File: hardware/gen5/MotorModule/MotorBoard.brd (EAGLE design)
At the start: 160 x 100 mm, 51 parts, among them IC2 3.3V REG, M1O1 TEST_PT, M1O2 TEST_PT, M1O3 TEST_PT

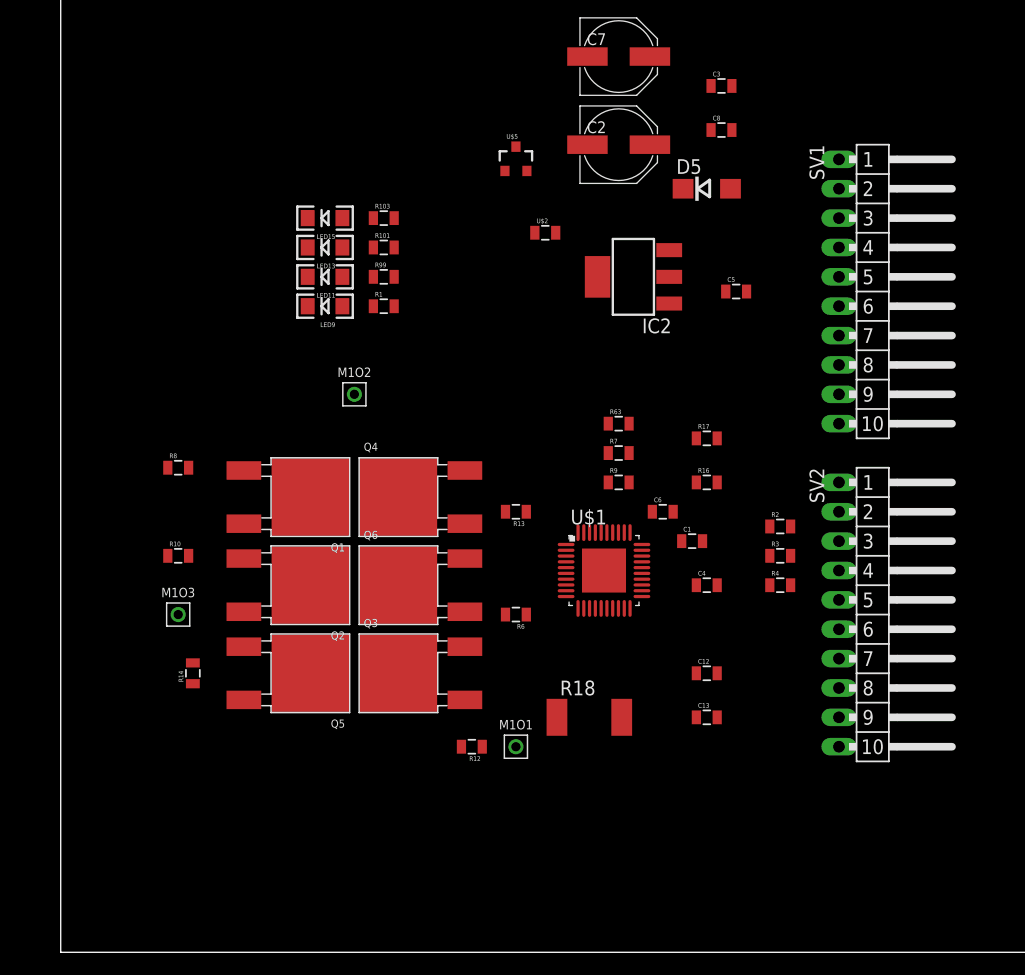
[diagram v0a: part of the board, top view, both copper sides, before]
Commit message: Working on motor board layout - should be done soon
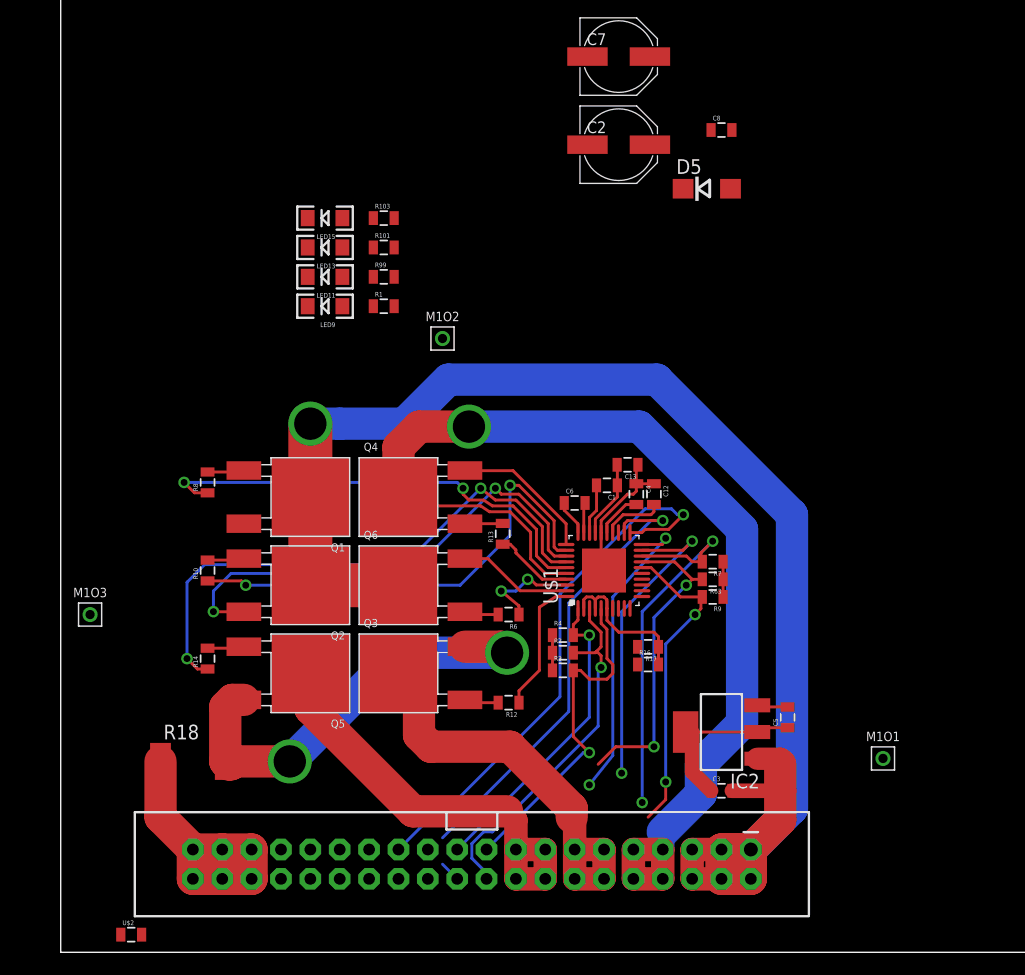
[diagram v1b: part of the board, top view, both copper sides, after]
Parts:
- removed SV1, SV2: (no value), con-lstb:MA10-1W
- removed U$5: MCP9700SMD, SparkFun-Sensors:SOT23-3
- added J1: M20X2SHROUDED, SparkFun-Connectors:2X20_SHROUDED
- moved U$2 70.5 mm to (6.10, 1.52)
- moved C3 61.0 mm to (57.1, 14.0)
- moved IC2 40.1 mm to (57.1, 19.1)
- moved C5 37.1 mm to (62.9, 20.3), turned to 90 degrees
- moved R18 34.5 mm to (11.4, 16.5)
- moved M1O1 31.8 mm to (71.1, 16.8)
- moved C13 22.9 mm to (49.0, 42.2), turned to 180 degrees
- moved R2 21.7 mm to (43.4, 25.9)
- moved R3 21.2 mm to (43.4, 24.4)
- moved R4 19.3 mm to (43.4, 27.4)
- moved R17 18.7 mm to (50.8, 26.4), turned to 180 degrees
- moved R16 16.5 mm to (50.8, 24.9)
- moved C12 16.2 mm to (51.3, 39.6), turned to 270 degrees
- moved R63 15.7 mm to (56.4, 32.3), turned to 180 degrees
- moved R9 12.8 mm to (56.4, 30.7), turned to 180 degrees
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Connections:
- removed net TSENSE: U$5.2
- net 12V: now also J1.1, J1.2, J1.3, J1.4, J1.5, J1.6; no longer SV1.10, SV1.6, SV1.7, SV1.8, SV1.9
- net 12VGND: now also J1.35, J1.36, J1.37, J1.38, J1.39, J1.40; no longer SV1.1, SV1.2, SV1.3, SV1.4, SV1.5
- net 3.3V: no longer U$5.1
- net 5V: now also J1.23
- net BRAKE: now also J1.27; no longer SV2.6
- net DIR: now also J1.25; no longer SV2.7
- net ENABLE: now also J1.22; no longer SV2.4
- net FAULTN: now also J1.31; no longer SV2.2
- net GND: no longer U$5.3
- net HALLOUT: now also J1.24; no longer SV2.3
- net LOCKN: now also J1.26; no longer SV2.1
- net M1H1: now also J1.19, R3.2; no longer R2.2, SV2.9
- net M1H2: now also J1.20, R2.2; no longer R3.2, SV2.10
- net M1H3: now also J1.21; no longer SV2.8
- net M1O1: now also J1.11, J1.12, J1.13, J1.14
- net M1O2: now also J1.10, J1.7, J1.8, J1.9
- net M1O3: now also J1.15, J1.16, J1.17, J1.18
- net PWM: now also J1.29; no longer SV2.5
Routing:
- net 12V: track 0.00 -> 142.2 mm, vias 0 -> 2
- net M1O2: track 0.00 -> 97.7 mm, vias 0 -> 1
- net M1O3: track 0.00 -> 79.9 mm, vias 0 -> 2
- net O1: track 0.00 -> 51.4 mm, vias 0 -> 2
- net N$17: track 0.00 -> 48.8 mm, vias 0 -> 2
- net DIR: track 0.00 -> 47.5 mm, vias 0 -> 1
- net M1O1: track 0.00 -> 45.6 mm
- net ENABLE: track 0.00 -> 41.9 mm, vias 0 -> 1
- net N$21: track 0.00 -> 40.9 mm, vias 0 -> 2
- net N$20: track 0.00 -> 40.3 mm, vias 0 -> 2
- net LOCKN: track 0.00 -> 32.8 mm, vias 0 -> 2
- net M1H2: track 0.00 -> 31.8 mm, vias 0 -> 1
- net M1H1: track 0.00 -> 30.0 mm, vias 0 -> 1
- net PWM: track 0.00 -> 27.3 mm, vias 0 -> 2
- net HALLOUT: track 0.00 -> 27.2 mm, vias 0 -> 2
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
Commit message: Motor board finished - needs review
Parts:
- removed M1O1, M1O2, M1O3: TEST_PT, gen3:TESTING_PT
- moved U$2 55.4 mm to (57.8, 21.5), turned to 270 degrees
- moved LED11 43.7 mm to (50.3, 24.4)
- moved R99 43.2 mm to (54.6, 24.4)
- moved LED13 40.4 mm to (54.1, 35.3)
- moved LED15 40.3 mm to (54.1, 38.1), turned to 0 degrees
- moved R101 40.1 mm to (54.6, 31.0), turned to 270 degrees
- moved D5 38.9 mm to (58.4, 27.2), turned to 270 degrees
- moved R103 34.6 mm to (50.3, 37.1), turned to 270 degrees
- moved C7 34.3 mm to (37.3, 45.0)
- moved LED9 27.5 mm to (47.0, 42.7)
- moved C8 27.5 mm to (43.9, 47.0), turned to 180 degrees
- moved C2 26.4 mm to (55.4, 44.5), turned to 180 degrees
- moved R1 26.2 mm to (48.5, 39.6), turned to 270 degrees
- moved R14 8.77 mm to (4.06, 23.9), flipped to the bottom
- moved R6 5.79 mm to (33.5, 26.7)
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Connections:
- net 12VGND: now also J1.22, J1.33, J1.34
- net ENABLE: now also J1.30; no longer J1.22
- net M1O1: no longer M1O1.P$1
- net M1O2: no longer M1O2.P$1
- net M1O3: no longer M1O3.P$1
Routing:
- net 12VGND: track 26.6 -> 183.1 mm
- net 5V: track 8.36 -> 79.7 mm, vias 0 -> 3
- net GND: track 27.1 -> 83.1 mm, vias 0 -> 2
- net FAULTN: track 27.1 -> 73.0 mm, vias 2 -> 3
- net M1O2: track 97.7 -> 136.5 mm
- net PWM: track 27.3 -> 63.8 mm, vias 2 -> 1
- net HALLOUT: track 27.2 -> 63.1 mm, vias 2 -> 4
- net BRAKE: track 26.2 -> 60.6 mm, vias 2 -> 1
- net O1: track 51.4 -> 84.3 mm, vias 2 -> 3
- net LOCKN: track 32.8 -> 65.2 mm
- net 12V: track 142.2 -> 171.6 mm, vias 2 -> 4
- net ENABLE: track 41.9 -> 70.0 mm, vias 1 -> 3
- net M1O3: track 79.9 -> 101.6 mm
- net M1O1: track 45.6 -> 61.9 mm, vias 0 -> 2
- net 3.3V: track 5.72 -> 20.1 mm
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- added copper zone on layer 1, net 12VGND
- added copper zone on layer 16, net 12VGND
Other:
- board size 160 x 100 mm -> 60.9 x 49.7 mm

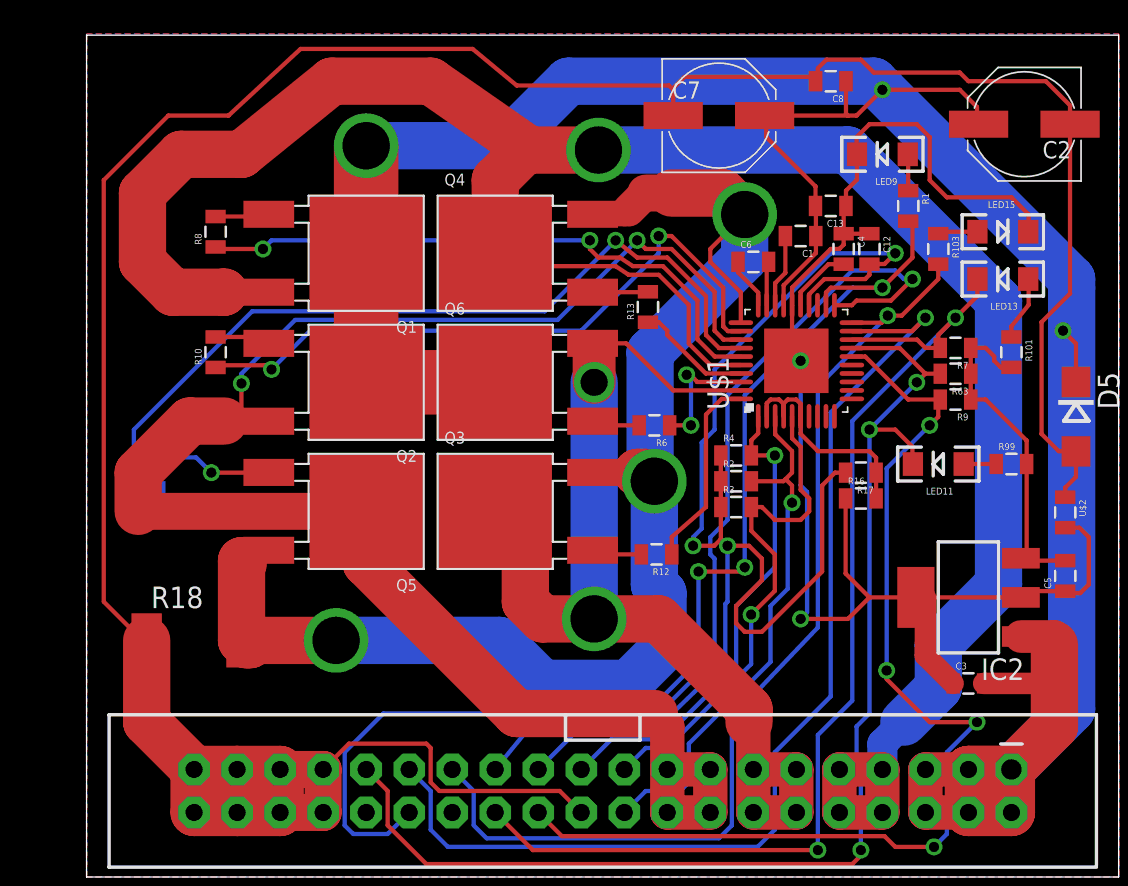
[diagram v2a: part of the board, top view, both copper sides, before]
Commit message: few minor motor board fixes
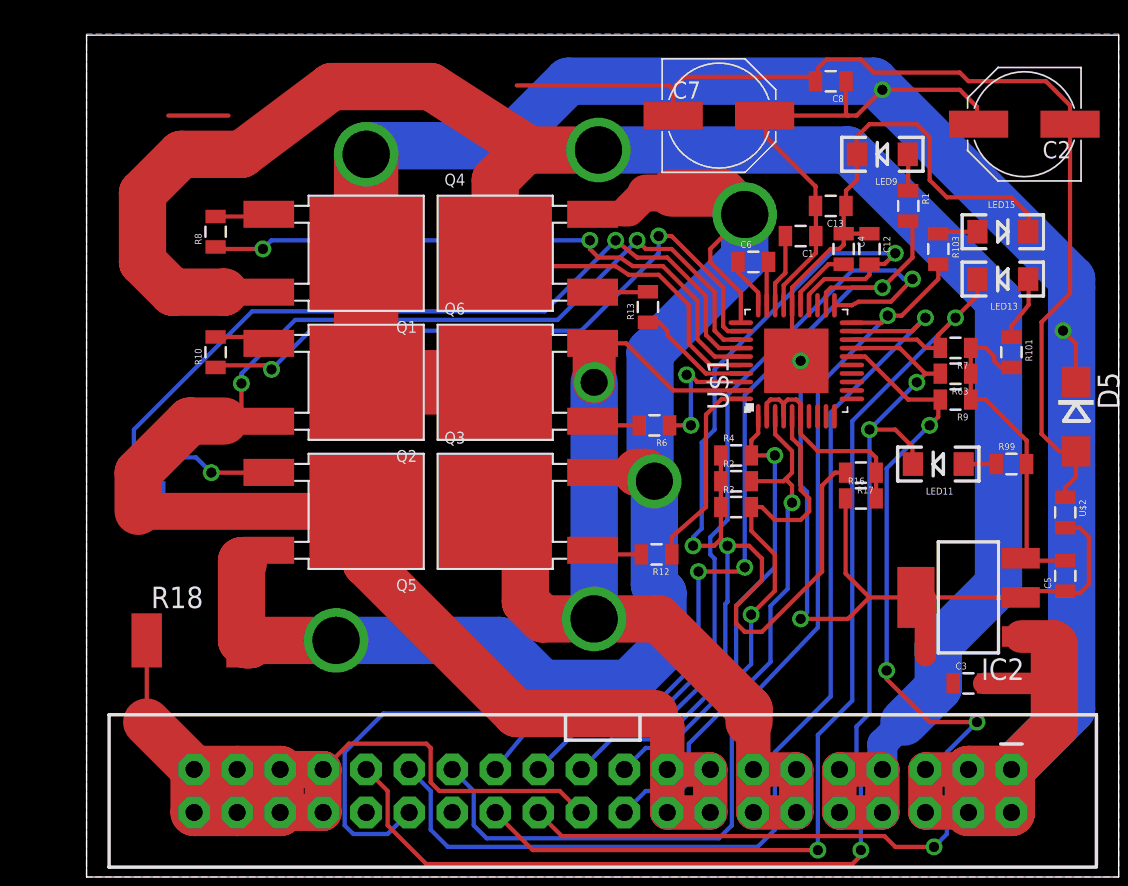
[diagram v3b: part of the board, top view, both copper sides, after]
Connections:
- net 12VGND: now also C3.1
- net GND: no longer C3.1
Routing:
- net 12VGND: track 183.1 -> 125.0 mm
- net GND: track 83.1 -> 80.8 mm
- net 12V: track 171.6 -> 171.3 mm, vias 4 -> 3
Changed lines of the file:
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@@
 <contactref element="C5" pad="1"/>
 <contactref element="U$2" pad="2"/>
-<contactref element="C3" pad="1"/>
 <contactref element="LED9" pad="C"/>
 <contactref element="LED15" pad="C"/>
 <wire x1="48.971" y1="16.51" x2="49.53" y2="16.51" width="0.254" layer="1"/>
 <wire x1="49.53" y1="16.51" x2="55.1688" y2="16.51" width="0.254" layer="1"/>
-<wire x1="51.17" y1="11.43" x2="49.53" y2="13.07" width="1.27" layer="1"/>
 <wire x1="49.53" y1="13.07" x2="49.53" y2="16.002" width="1.27" layer="1"/>
 <wire x1="49.53" y1="16.002" x2="49.53" y2="16.51" width="1.27" layer="1"/>
@@
 <wire x1="24.13" y1="29.21" x2="16.51" y2="29.21" width="3.81" layer="1"/>
 <wire x1="16.51" y1="29.21" x2="16.51" y2="36.83" width="3.81" layer="1"/>
-<wire x1="16.51" y1="36.83" x2="16.51" y2="43.18" width="3.81" layer="1"/>
-<via x="16.51" y="43.18" extent="1-16" drill="2.8"/>
+<wire x1="16.51" y1="36.83" x2="16.51" y2="42.672" width="3.81" layer="1"/>
+<via x="16.51" y="42.672" extent="1-16" drill="2.8"/>
 <wire x1="41.16" y1="33.759" x2="41.16" y2="34.937" width="0.254" layer="1"/>
 <wire x1="41.16" y1="34.937" x2="43.064" y2="36.841" width="0.254" layer="1"/>
@@
 <wire x1="54.356" y1="6.35" x2="54.61" y2="6.096" width="2.794" layer="1"/>
 <wire x1="54.61" y1="6.096" x2="54.61" y2="6.35" width="2.794" layer="1"/>
-<via x="54.61" y="6.35" extent="1-16" drill="1.2" shape="octagon"/>
 <wire x1="54.61" y1="6.35" x2="58.166" y2="9.906" width="2.794" layer="16"/>
 <wire x1="58.166" y1="9.906" x2="58.166" y2="34.798" width="2.794" layer="16"/>
@@
 <wire x1="46.482" y1="46.99" x2="28.448" y2="46.99" width="2.794" layer="16"/>
 <wire x1="28.448" y1="46.99" x2="24.638" y2="43.18" width="2.794" layer="16"/>
-<wire x1="24.638" y1="43.18" x2="16.51" y2="43.18" width="2.794" layer="16"/>
 <via x="46.99" y="46.482" extent="1-16" drill="0.6"/>
 <wire x1="43.042" y1="39.624" x2="43.042" y2="40.778" width="0.254" layer="1"/>
@@
 <wire x1="44.842" y1="46.99" x2="44.842" y2="45.074" width="0.254" layer="1"/>
 <wire x1="44.842" y1="45.074" x2="44.958" y2="44.958" width="0.254" layer="1"/>
+<wire x1="16.51" y1="42.672" x2="17.018" y2="43.18" width="2.794" layer="16"/>
+<wire x1="17.018" y1="43.18" x2="24.638" y2="43.18" width="2.794" layer="16"/>
 </signal>
 <signal name="12VGND">
@@
 <wire x1="8.89" y1="6.35" x2="6.35" y2="6.35" width="2.794" layer="1"/>
 <wire x1="8.89" y1="6.35" x2="8.89" y2="3.81" width="2.794" layer="1"/>
-<wire x1="3.55" y1="13.97" x2="3.55" y2="9.15" width="2.794" layer="1"/>
 <wire x1="3.55" y1="9.15" x2="6.35" y2="6.35" width="2.794" layer="1"/>
 <contactref element="J1" pad="22"/>
@@
 <wire x1="6.35" y1="6.604" x2="3.556" y2="9.398" width="0.254" layer="1"/>
 <wire x1="3.556" y1="9.398" x2="3.556" y2="13.716" width="0.254" layer="1"/>
-<wire x1="3.556" y1="13.716" x2="1.016" y2="16.256" width="0.254" layer="1"/>
-<wire x1="1.016" y1="16.256" x2="1.016" y2="41.148" width="0.254" layer="1"/>
-<wire x1="1.016" y1="41.148" x2="4.826" y2="44.958" width="0.254" layer="1"/>
 <wire x1="4.826" y1="44.958" x2="8.382" y2="44.958" width="0.254" layer="1"/>
-<wire x1="8.382" y1="44.958" x2="12.6365" y2="48.895" width="0.254" layer="1"/>
-<wire x1="12.6365" y1="48.895" x2="22.7965" y2="48.895" width="0.254" layer="1"/>
-<wire x1="22.7965" y1="48.895" x2="25.4" y2="46.736" width="0.254" layer="1"/>
 <wire x1="25.4" y1="46.736" x2="34.384" y2="46.736" width="0.254" layer="1"/>
 <wire x1="34.384" y1="46.736" x2="34.638" y2="46.482" width="0.254" layer="1"/>
@@
 <vertex x="60.96" y="49.784"/>
 </polygon>
+<contactref element="C3" pad="1"/>
 </signal>
 <signal name="M1O1">
@@
 <wire x1="3.302" y1="40.386" x2="5.588" y2="42.672" width="2.794" layer="1"/>
 <wire x1="5.588" y1="42.672" x2="9.144" y2="42.672" width="2.794" layer="1"/>
-<wire x1="9.144" y1="42.672" x2="14.478" y2="46.99" width="2.794" layer="1"/>
-<wire x1="14.478" y1="46.99" x2="20.32" y2="46.99" width="2.794" layer="1"/>
-<wire x1="20.32" y1="46.99" x2="26.162" y2="42.926" width="2.794" layer="1"/>
+<wire x1="9.144" y1="42.672" x2="14.478" y2="46.6725" width="2.794" layer="1"/>
+<wire x1="14.478" y1="46.6725" x2="20.32" y2="46.6725" width="2.794" layer="1"/>
+<wire x1="20.32" y1="46.6725" x2="26.162" y2="42.926" width="2.794" layer="1"/>
 <wire x1="5.094" y1="34.53" x2="8.114" y2="34.53" width="2.794" layer="1"/>
 <wire x1="8.114" y1="34.53" x2="8.128" y2="34.544" width="2.794" layer="1"/>
@@
 <wire x1="24.384" y1="13.97" x2="14.732" y2="13.97" width="2.794" layer="16"/>
 <wire x1="33.006" y1="23.89" x2="33.528" y2="23.368" width="2.794" layer="1"/>
-<via x="33.528" y="23.368" extent="1-16" drill="2.8"/>
+<via x="33.528" y="23.368" extent="1-16" drill="2.2"/>
 <wire x1="33.528" y1="23.368" x2="33.274" y2="23.622" width="2.794" layer="16"/>
 <wire x1="33.274" y1="23.622" x2="33.274" y2="30.988" width="2.794" layer="16"/>
@@
 <wire x1="47.752" y1="35.814" x2="45.212" y2="35.814" width="0.254" layer="16"/>
 <wire x1="45.212" y1="35.814" x2="37.846" y2="28.448" width="0.254" layer="16"/>
-<wire x1="48.768" y1="35.306" x2="47.498" y2="34.036" width="0.254" layer="1"/>
-<wire x1="47.498" y1="34.036" x2="45.466" y2="34.036" width="0.254" layer="1"/>
-<wire x1="45.466" y1="34.036" x2="45.189" y2="33.759" width="0.254" layer="1"/>
+<wire x1="48.768" y1="35.306" x2="47.498" y2="33.9725" width="0.254" layer="1"/>
+<wire x1="47.498" y1="33.9725" x2="45.593" y2="33.9725" width="0.254" layer="1"/>
+<wire x1="45.593" y1="33.9725" x2="45.189" y2="33.759" width="0.254" layer="1"/>
 <wire x1="45.189" y1="33.759" x2="44.16" y2="33.759" width="0.254" layer="1"/>
 <wire x1="33.274" y1="9.144" x2="26.416" y2="9.144" width="0.254" layer="16"/>
